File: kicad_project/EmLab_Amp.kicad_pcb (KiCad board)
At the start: 4 copper layers, 118.1 x 58 mm, 183 parts, among them J1 JTAG, J2 USB_C_Receptacle, J3 GPIO_EXP, J4 BNC, U1 TPS7A80, U10 THS4131ID, U11 THS4131ID, U12 THS4131ID, U2 LT3094xDD, U3 LT3045xDD, U4 TPS6513x, U5 LPC4370-TFBGA100, U6 IS25LP080D, U7 ADR421, U8 MCP601R, U9 LMH6518, Y1 12MHz Crystal

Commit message: wolololo
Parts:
- removed G***: LOGO, LoaDy:FI_LOGO_11x10mm
- removed the REF** at (85.3, 114.7)
- removed the REF** at (85.3, 64.5)
- removed the REF** at (195.6, 114.7)
- removed the REF** at (195.6, 64.5)
- D1, D2: footprint Diode_SMD:D_SMA -> Diode_SMD:D_SOD-123
- J2: value USB_C_Receptacle -> USB_C_Receptacle_USB2.0
- JP1: footprint Connector_PinHeader_2.54mm:PinHeader_1x02_P2.54mm_Vertical_SMD_Pin1Left -> Connector_PinHeader_2.54mm:PinHeader_1x02_P2.54mm_Vertical_SMD_Pin1Right
- R41, R42: value 4K -> 40K
- U1: footprint Package_SON:WSON-8-1EP_3x3mm_P0.5mm_EP1.6x2.0mm -> LoaDy:TI-VSON-8
- U9: footprint Package_DFN_QFN:QFN-16-1EP_3x3mm_P0.5mm_EP2.7x2.7mm_ThermalVias -> LoaDy:QFN-16-1EP_4x4mm_P0.5mm_EP2.6x2.6mm
- moved L1 3.00 mm to (191.3, 108.0)
- moved D1 2.70 mm to (189.2, 112.3)
- moved L2 2.25 mm to (186.2, 97.0), turned to 90 degrees
- moved D2 1.43 mm to (181.6, 98.8)
- moved C58 0.76 mm to (128.4, 108.5)
- moved R25 0.76 mm to (130.4, 109.5)
- moved R26 0.76 mm to (130.4, 108.5)
- moved R30 0.76 mm to (128.4, 109.5)
- moved TP7 0.76 mm to (128.0, 112.8)
- moved C52 0.76 mm to (130.4, 107.4)
- moved C59 0.76 mm to (128.4, 107.4)
- moved C4 0.51 mm to (179.2, 70.9)
- moved C56 0.25 mm to (125.6, 99.6)
- moved C57 0.25 mm to (127.6, 99.6)
- moved C54 0.25 mm to (125.6, 100.6)
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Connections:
- U4 pad 25: (no net) -> GND
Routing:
- net /LPC4370-USB/USB_VBUS: track 14.7 -> 18.9 mm, vias 20 -> 21
- net /LPC4370-GPIO/BOOT_2: track 20.6 -> 23.8 mm
- net +3V3: track 166.4 -> 168.6 mm
- net /Power/VPOS: track 10.9 -> 12.2 mm
- net /Amplifier/S3_CS: track 58.6 -> 59.8 mm
- net GND: track 78.3 -> 79.3 mm, vias 236 -> 259
- net /Power/VNEG: track 10.1 -> 11.0 mm
- net /Amplifier/V_REF: track 54.9 -> 54.0 mm
- net /Amplifier/S3_SCLK: track 59.4 -> 60.4 mm
- net /Amplifier/S3_DIO: track 35.8 -> 36.7 mm
- net (no net): vias 4 -> 0
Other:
- board text added: "80dB Amp + Digitizer Rev. 2 Oldřich Pecák FI MUNI, September 2019"
- board text removed: "80dB Amp + Digitizer Rev. 1 Oldřich Pecák FI MUNI, May 2019"

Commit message: Rev 2
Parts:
- removed JP2: Jumper_3_Open, Jumper:SolderJumper-3_P1.3mm_Open_RoundedPad1.0x1.5mm
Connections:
- U5 pad H4: /Amplifier/S3_SCLK -> Net-(U5-PadH4)
- U5 pad J1: /LPC4370-GPIO/SSP1_MISO -> /Amplifier/S3_SCLK
- U5 pad J2: /LPC4370-GPIO/SSP1_MOSI -> /Amplifier/S3_DIO
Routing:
- net /LPC4370-GPIO/SSP1_MOSI: track 26.0 -> 0.00 mm, vias 2 -> 0
- net /LPC4370-GPIO/SSP1_MISO: track 25.3 -> 0.00 mm, vias 2 -> 0
- net /Amplifier/S3_DIO: track 36.7 -> 61.3 mm
- net +3V3: track 168.6 -> 170.6 mm
- net /Amplifier/S3_SCLK: track 60.4 -> 62.1 mm
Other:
- board text removed: "MISO"
- board text removed: "MOSI"

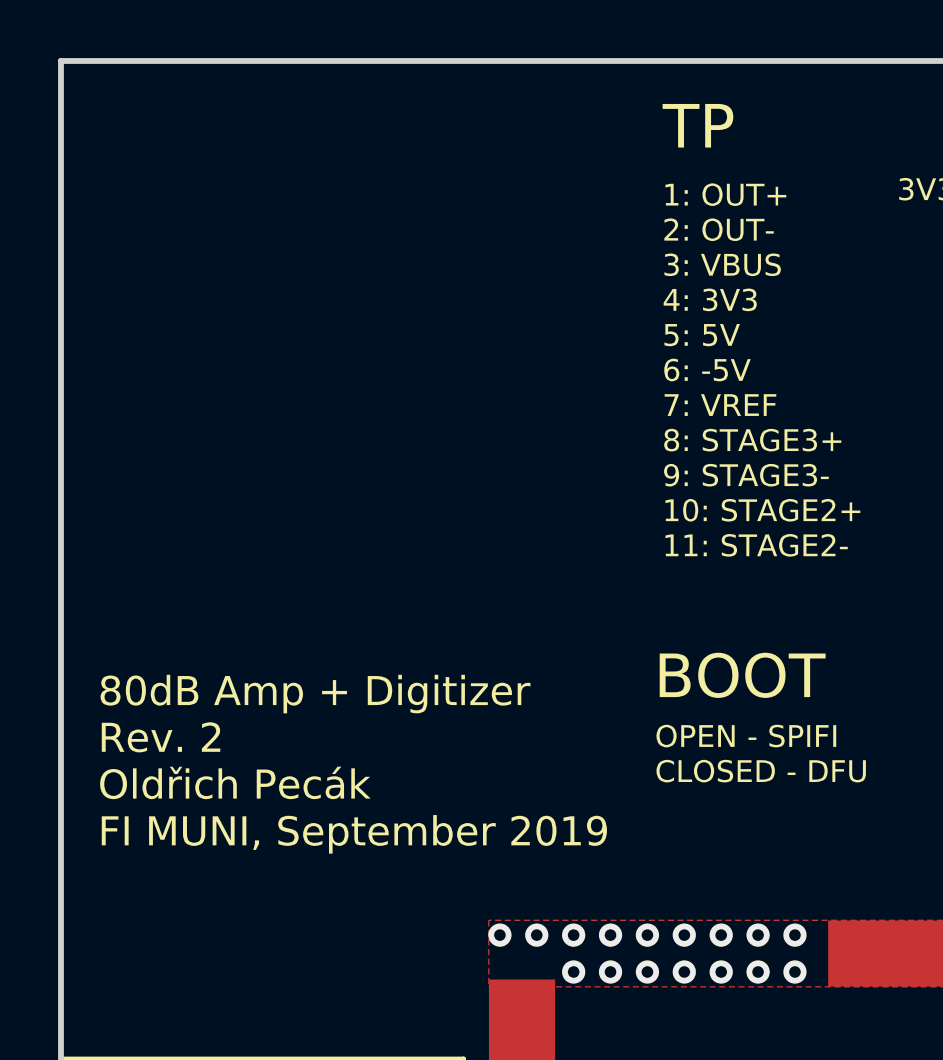
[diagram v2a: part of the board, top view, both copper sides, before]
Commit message: iBom + formatting PCB
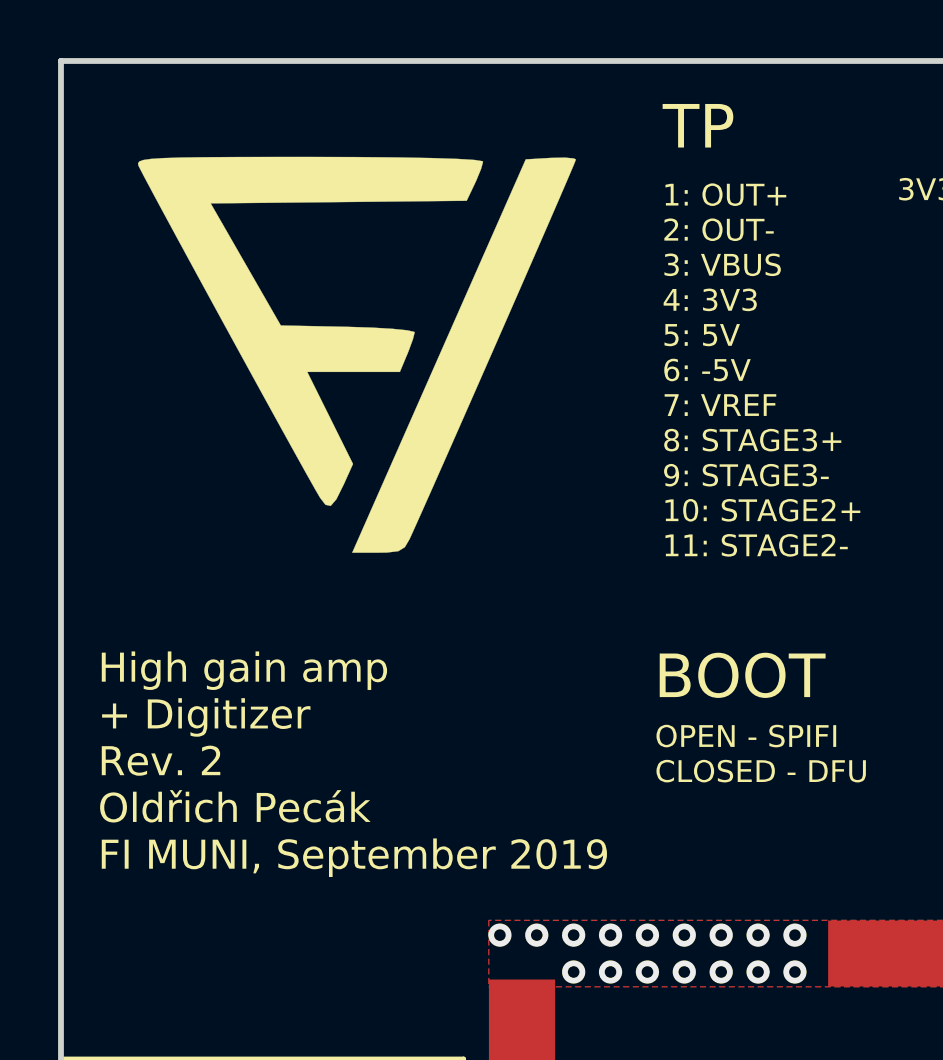
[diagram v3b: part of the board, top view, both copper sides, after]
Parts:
- added G***: LOGO, LoaDy:FI_LOGO_15x14mm, F.Cu at (91.6, 70.6)
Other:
- board text added: "High gain amp + Digitizer Rev. 2 Oldřich Pecák FI MUNI, September 2019"
- board text removed: "80dB Amp + Digitizer Rev. 2 Oldřich Pecák FI MUNI, September 2019"

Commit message: rev 2.1
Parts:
- added SW1: RST BTN, Button_Switch_SMD:SW_SPST_PTS810, F.Cu at (136.3, 85.5)
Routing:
- net /LPC4370-JTAG-PWR-MISC/RESET: track 27.2 -> 37.1 mm
- net GND: track 79.3 -> 85.0 mm, vias 259 -> 260
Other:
- board text added: "High gain amp + Digitizer Rev. 2.1 Oldřich Pecák FI MUNI, September 2019"
- board text removed: "High gain amp + Digitizer Rev. 2 Oldřich Pecák FI MUNI, September 2019"
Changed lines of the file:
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@@
-(kicad_pcb (version 20171130) (host pcbnew 5.0.2+dfsg1-1~bpo9+1)
+(kicad_pcb (version 20171130) (host pcbnew 5.1.4-e60b266~84~ubuntu19.04.1)
   (general
     (thickness 1.6)
     (drawings 33)
-    (tracks 1496)
+    (tracks 1503)
     (zones 0)
-    (modules 178)
+    (modules 179)
     (nets 161)
   )
@@
   (title_block
     (title "High gain amp + Digitizer")
-    (date 2019-09-23)
-    (rev 2)
+    (date 2019-10-11)
+    (rev 2.1)
     (company "Oldřich Pecák")
     (comment 1 "FI MUNI")
@@
   )
   (setup
-    (last_trace_width 0.2)
+    (last_trace_width 0.125)
     (user_trace_width 0.125)
     (user_trace_width 0.244)
@@
     (zone_45_only no)
     (trace_min 0.125)
-    (segment_width 0.15)
-    (edge_width 0.2)
     (via_size 0.4)
     (via_drill 0.2)
@@
     (uvia_min_size 0.4)
     (uvia_min_drill 0.2)
+    (edge_width 0.2)
+    (segment_width 0.15)
     (pcb_text_width 0.3)
     (pcb_text_size 1.5 1.5)
@@
     (mod_text_size 0.75 0.75)
     (mod_text_width 0.135)
-    (pad_size 2.6 2.6)
+    (pad_size 1.05 1)
     (pad_drill 0)
     (pad_to_mask_clearance 0.1)
@@
     (add_net "Net-(U7-Pad8)")
   )
+  (module Button_Switch_SMD:SW_SPST_PTS810 (layer F.Cu)
+    (at 136.314 85.53)
+    (descr "C&K Components, PTS 810 Series, Microminiature SMT Top Actuated, http://www.ckswitches.com/media/1476/pts810.pdf")
+    (tags "SPST Button Switch")
+    (attr smd)
+    (fp_text reference SW1 (at -4.234 1.084) (layer F.SilkS)
+      (effects (font (size 1 1) (thickness 0.15)))
+    )
+    (fp_text value "RST BTN" (at 0 2.6) (layer F.Fab)
+      (effects (font (size 1 1) (thickness 0.15)))
+    )
+    (fp_arc (start 0.4 0) (end 0.4 -1.1) (angle 180) (layer F.Fab) (width 0.1))
+    (fp_line (start 2.1 1.6) (end 2.1 -1.6) (layer F.Fab) (width 0.1))
+    (fp_line (start 2.1 -1.6) (end -2.1 -1.6) (layer F.Fab) (width 0.1))
+    (fp_line (start -2.1 -1.6) (end -2.1 1.6) (layer F.Fab) (width 0.1))
+    (fp_line (start -2.1 1.6) (end 2.1 1.6) (layer F.Fab) (width 0.1))
+    (fp_arc (start -0.4 0) (end -0.4 1.1) (angle 180) (layer F.Fab) (width 0.1))
+    (fp_line (start -0.4 -1.1) (end 0.4 -1.1) (layer F.Fab) (width 0.1))
+    (fp_line (start 0.4 1.1) (end -0.4 1.1) (layer F.Fab) (width 0.1))
+    (fp_line (start 2.2 -1.7) (end -2.2 -1.7) (layer F.SilkS) (width 0.12))
+    (fp_line (start -2.2 -1.7) (end -2.2 -1.58) (layer F.SilkS) (width 0.12))
+    (fp_line (start -2.2 -0.57) (end -2.2 0.57) (layer F.SilkS) (width 0.12))
+    (fp_line (start -2.2 1.58) (end -2.2 1.7) (layer F.SilkS) (width 0.12))
+    (fp_line (start -2.2 1.7) (end 2.2 1.7) (layer F.SilkS) (width 0.12))
+    (fp_line (start 2.2 1.7) (end 2.2 1.58) (layer F.SilkS) (width 0.12))
+    (fp_line (start 2.2 0.57) (end 2.2 -0.57) (layer F.SilkS) (width 0.12))
+    (fp_line (start 2.2 -1.58) (end 2.2 -1.7) (layer F.SilkS) (width 0.12))
+    (fp_text user %R (at 0 0) (layer F.Fab)
+      (effects (font (size 0.6 0.6) (thickness 0.09)))
+    )
+    (fp_line (start 2.85 -1.85) (end 2.85 1.85) (layer F.CrtYd) (width 0.05))
+    (fp_line (start 2.85 1.85) (end -2.85 1.85) (layer F.CrtYd) (width 0.05))
+    (fp_line (start -2.85 1.85) (end -2.85 -1.85) (layer F.CrtYd) (width 0.05))
+    (fp_line (start -2.85 -1.85) (end 2.85 -1.85) (layer F.CrtYd) (width 0.05))
+    (pad 2 smd rect (at 2.075 1.075) (size 1.05 1) (layers F.Cu F.Paste F.Mask)
+      (net 19 GND))
+    (pad 2 smd rect (at -2.075 1.075) (size 1.05 1) (layers F.Cu F.Paste F.Mask)
+      (net 19 GND))
+    (pad 1 smd rect (at 2.075 -1.075) (size 1.05 1) (layers F.Cu F.Paste F.Mask)
+      (net 52 /LPC4370-JTAG-PWR-MISC/RESET))
+    (pad 1 smd rect (at -2.075 -1.075) (size 1.05 1) (layers F.Cu F.Paste F.Mask)
+      (net 52 /LPC4370-JTAG-PWR-MISC/RESET))
+    (model ${KISYS3DMOD}/Button_Switch_SMD.3dshapes/SW_SPST_PTS810.wrl
+      (at (xyz 0 0 0))
+      (scale (xyz 1 1 1))
+      (rotate (xyz 0 0 0))
+    )
+  )
   (module Connector_PinHeader_2.54mm:PinHeader_1x02_P2.54mm_Vertical_SMD_Pin1Right (layer F.Cu)
     (at 145.9357 63.9445 180)
@@
       (xy 7.192878 -6.705129) (xy 7.505862 -6.67553)) (layer F.SilkS) (width 0.01))
   )
-  (gr_text "High gain amp\n+ Digitizer\nRev. 2\nOldřich Pecák\nFI MUNI, September 2019" (at 82.677 84.709) (layer F.SilkS)
+  (gr_text "High gain amp\n+ Digitizer\nRev. 2.1\nOldřich Pecák\nFI MUNI, September 2019" (at 82.677 84.709) (layer F.SilkS)
     (effects (font (size 1 1) (thickness 0.2)) (justify left))
   )
@@
   (segment (start 149.7965 62.6745) (end 149.86 62.738) (width 0.244) (layer F.Cu) (net 19))
   (segment (start 147.5907 62.6745) (end 149.7965 62.6745) (width 0.244) (layer F.Cu) (net 19))
+  (via (at 138.43 88.138) (size 0.8) (drill 0.4) (layers F.Cu B.Cu) (net 19))
+  (segment (start 138.389 86.605) (end 138.389 88.097) (width 0.5) (layer F.Cu) (net 19))
+  (segment (start 138.389 88.097) (end 138.43 88.138) (width 0.5) (layer F.Cu) (net 19))
+  (segment (start 138.389 86.605) (end 134.239 86.605) (width 0.5) (layer F.Cu) (net 19))
   (segment (start 189.0085 103.255) (end 189.607 103.255) (width 0.23) (layer F.Cu) (net 20))
   (segment (start 189.865 102.997) (end 190.754 102.997) (width 0.23) (layer F.Cu) (net 20))
@@
   (segment (start 146.882001 82.924801) (end 146.6723 82.7151) (width 0.125) (layer F.Cu) (net 52))
   (segment (start 146.6723 82.7151) (end 144.8943 82.7151) (width 0.125) (layer F.Cu) (net 52))
+  (segment (start 138.4271 84.4931) (end 138.389 84.455) (width 0.125) (layer F.Cu) (net 52))
+  (segment (start 144.1323 84.4931) (end 138.4271 84.4931) (width 0.125) (layer F.Cu) (net 52))
+  (segment (start 138.389 84.455) (end 134.239 84.455) (width 0.125) (layer F.Cu) (net 52))
   (segment (start 150.0948 81.437468) (end 149.6949 81.837368) (width 0.125) (layer F.Cu) (net 53))
   (segment (start 150.0948 81.3622) (end 150.0948 81.437468) (width 0.125) (layer F.Cu) (net 53))
